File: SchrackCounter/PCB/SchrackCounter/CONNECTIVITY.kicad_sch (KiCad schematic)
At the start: 24 parts, among them J1 TYPE-C-31-M-12 (USB C CONN), U7 USBLC6-2SC6

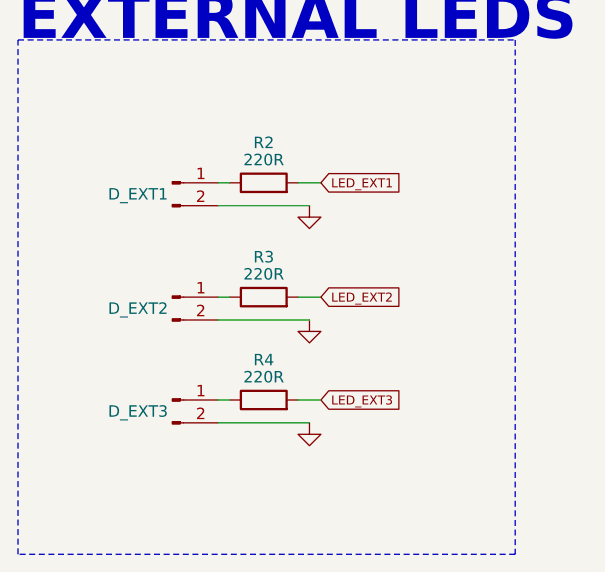
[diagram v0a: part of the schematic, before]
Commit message: SchrackMulticlock and Counter update
Schematic update for both
PCB update for Counter
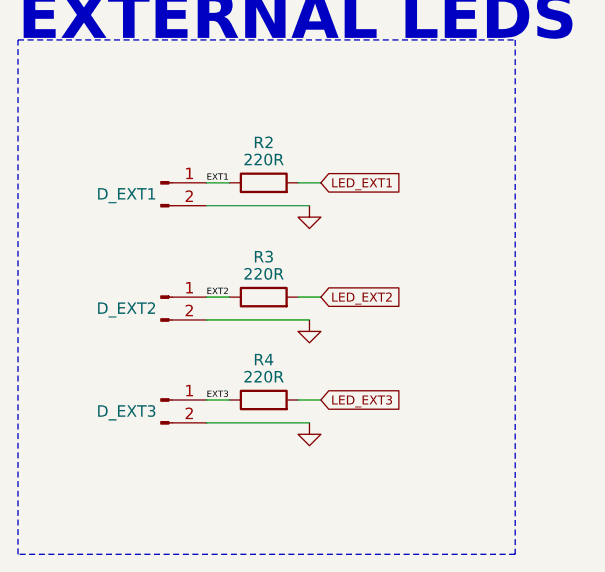
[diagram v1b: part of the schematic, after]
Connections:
- net EXT1: now reaches D_EXT1.1 (Pin_1), R2.1
- net EXT3: now reaches D_EXT3.1 (Pin_1), R4.1
- net EXT2: now reaches D_EXT2.1 (Pin_1), R3.1
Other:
- moved on the sheet: D_EXT1, D_EXT2, D_EXT3
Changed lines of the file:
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@@
 	(wire
 		(pts
-			(xy 78.74 142.24) (xy 77.47 142.24)
+			(xy 78.74 142.24) (xy 76.2 142.24)
 		)
 		(stroke
@@
 	(wire
 		(pts
-			(xy 78.74 118.11) (xy 77.47 118.11)
-		)
-		(stroke
-			(width 0)
-			(type default)
-		)
-	)
-	(wire
-		(pts
-			(xy 77.47 120.65) (xy 87.63 120.65)
+			(xy 76.2 120.65) (xy 87.63 120.65)
 		)
 		(stroke
@@
 	(wire
 		(pts
-			(xy 77.47 133.35) (xy 87.63 133.35)
+			(xy 76.2 133.35) (xy 87.63 133.35)
 		)
 		(stroke
@@
 	(wire
 		(pts
-			(xy 222.25 49.53) (xy 223.52 49.53)
+			(xy 76.2 118.11) (xy 78.74 118.11)
 		)
 		(stroke
@@
 	(wire
 		(pts
-			(xy 78.74 130.81) (xy 77.47 130.81)
+			(xy 222.25 49.53) (xy 223.52 49.53)
 		)
 		(stroke
@@
 	(wire
 		(pts
+			(xy 76.2 130.81) (xy 78.74 130.81)
+		)
+		(stroke
+			(width 0)
+			(type default)
+		)
+	)
+	(wire
+		(pts
 			(xy 223.52 137.16) (xy 223.52 147.32)
 		)
@@
 	(wire
 		(pts
-			(xy 77.47 144.78) (xy 87.63 144.78)
+			(xy 76.2 144.78) (xy 87.63 144.78)
 		)
 		(stroke
@@
 		)
 	)
+	(label "EXT2"
+		(at 76.2 130.81 0)
+		(fields_autoplaced yes)
+		(effects
+			(font
+				(size 0.7 0.7)
+			)
+			(justify left bottom)
+		)
+	)
+	(label "EXT3"
+		(at 76.2 142.24 0)
+		(fields_autoplaced yes)
+		(effects
+			(font
+				(size 0.7 0.7)
+			)
+			(justify left bottom)
+		)
+	)
+	(label "EXT1"
+		(at 76.2 118.11 0)
+		(fields_autoplaced yes)
+		(effects
+			(font
+				(size 0.7 0.7)
+			)
+			(justify left bottom)
+		)
+	)
 	(global_label "VBUS 5V"
 		(shape input)
@@
 	(symbol
 		(lib_id "Connector:Conn_01x02_Pin")
-		(at 72.39 118.11 0)
+		(at 71.12 118.11 0)
 		(unit 1)
 		(exclude_from_sim no)
@@
 		(dnp no)
 		(property "Reference" "D_EXT1"
-			(at 68.58 119.38 0)
+			(at 67.31 119.38 0)
 			(effects
 				(font
@@
 		)
 		(property "Value" "Conn_01x02_Pin"
-			(at 71.755 115.57 0)
+			(at 70.485 115.57 0)
 			(effects
 				(font
@@
 		)
 		(property "Footprint" "Connector_JST:JST_XH_B2B-XH-A_1x02_P2.50mm_Vertical"
-			(at 72.39 118.11 0)
+			(at 71.12 118.11 0)
 			(effects
 				(font
@@
 		)
 		(property "Datasheet" "~"
-			(at 72.39 118.11 0)
+			(at 71.12 118.11 0)
 			(effects
 				(font
@@
 		)
 		(property "Description" "Generic connector, single row, 01x02, script generated"
-			(at 72.39 118.11 0)
+			(at 71.12 118.11 0)
 			(effects
 				(font
@@
 	(symbol
 		(lib_id "Connector:Conn_01x02_Pin")
-		(at 72.39 142.24 0)
+		(at 71.12 142.24 0)
 		(unit 1)
 		(exclude_from_sim no)
@@
 		(dnp no)
 		(property "Reference" "D_EXT3"
-			(at 68.58 143.51 0)
+			(at 67.31 143.51 0)
 			(effects
 				(font
@@
 		)
 		(property "Value" "Conn_01x02_Pin"
-			(at 71.755 139.7 0)
+			(at 70.485 139.7 0)
 			(effects
 				(font
@@
 		)
 		(property "Footprint" "Connector_JST:JST_XH_B2B-XH-A_1x02_P2.50mm_Vertical"
-			(at 72.39 142.24 0)
+			(at 71.12 142.24 0)
 			(effects
 				(font
@@
 		)
 		(property "Datasheet" "~"
-			(at 72.39 142.24 0)
+			(at 71.12 142.24 0)
 			(effects
 				(font
@@
 		)
 		(property "Description" "Generic connector, single row, 01x02, script generated"
-			(at 72.39 142.24 0)
+			(at 71.12 142.24 0)
 			(effects
 				(font
@@
 	(symbol
 		(lib_id "Connector:Conn_01x02_Pin")
-		(at 72.39 130.81 0)
+		(at 71.12 130.81 0)
 		(unit 1)
 		(exclude_from_sim no)
@@
 		(dnp no)
 		(property "Reference" "D_EXT2"
-			(at 68.58 132.08 0)
+			(at 67.31 132.08 0)
 			(effects
 				(font
@@
 		)
 		(property "Value" "Conn_01x02_Pin"
-			(at 71.755 128.27 0)
+			(at 70.485 128.27 0)
 			(effects
 				(font
@@
 		)
 		(property "Footprint" "Connector_JST:JST_XH_B2B-XH-A_1x02_P2.50mm_Vertical"
-			(at 72.39 130.81 0)
+			(at 71.12 130.81 0)
 			(effects
 				(font
@@
 		)
 		(property "Datasheet" "~"
-			(at 72.39 130.81 0)
+			(at 71.12 130.81 0)
 			(effects
 				(font
@@
 		)
 		(property "Description" "Generic connector, single row, 01x02, script generated"
-			(at 72.39 130.81 0)
+			(at 71.12 130.81 0)
 			(effects
 				(font

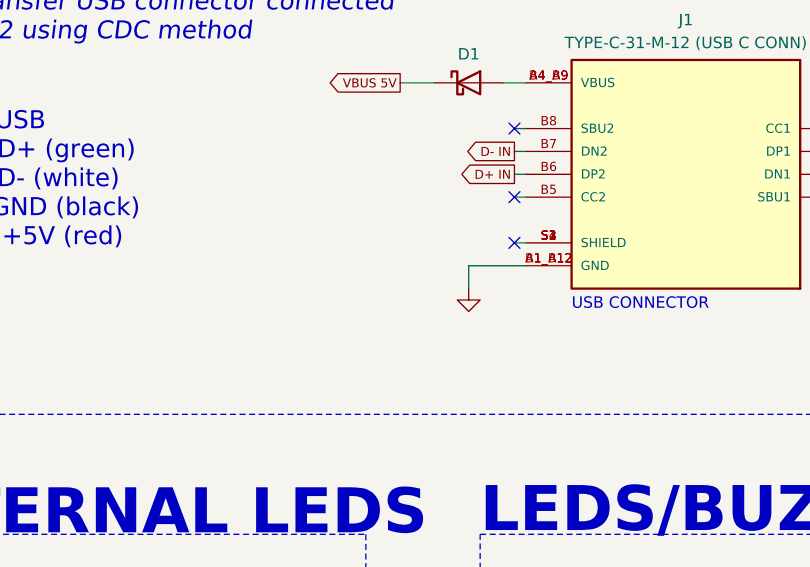
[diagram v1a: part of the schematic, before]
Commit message: Schrackcounter Prototype update
Schematic + PCB update, final version
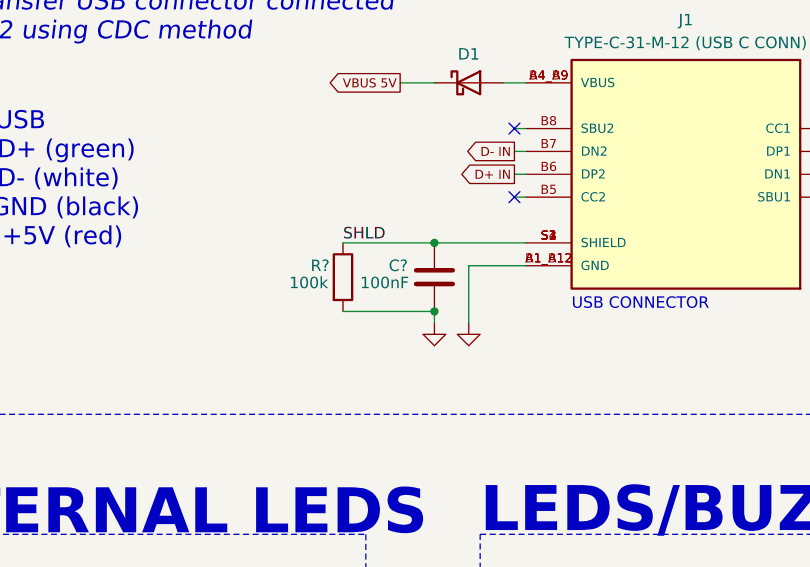
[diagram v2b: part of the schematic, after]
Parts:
- added C?: 100nF, Capacitor_SMD:C_0805_2012Metric_Pad1.18x1.45mm_HandSolder, symbol Device:C
- added R?: 100k, Resistor_SMD:R_0805_2012Metric_Pad1.20x1.40mm_HandSolder, symbol Device:R
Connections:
- net GND: now also C?.1, R?.2
- net SHLD: now reaches J1.S1 (SHIELD), J1.S2 (SHIELD), J1.S3 (SHIELD), J1.S4 (SHIELD)
- net SHLD: now also C?.2, R?.1
- no-connect marks 5 -> 4

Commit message: SchrackMulticlock update
Schematic and PCB update
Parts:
- gave numbers to parts that had none: 2
- renumbered C9 to C10, R9 to R10, R10 to R11, R11 to R12, R5 to R6, R6 to R7, R7 to R8, R8 to R9

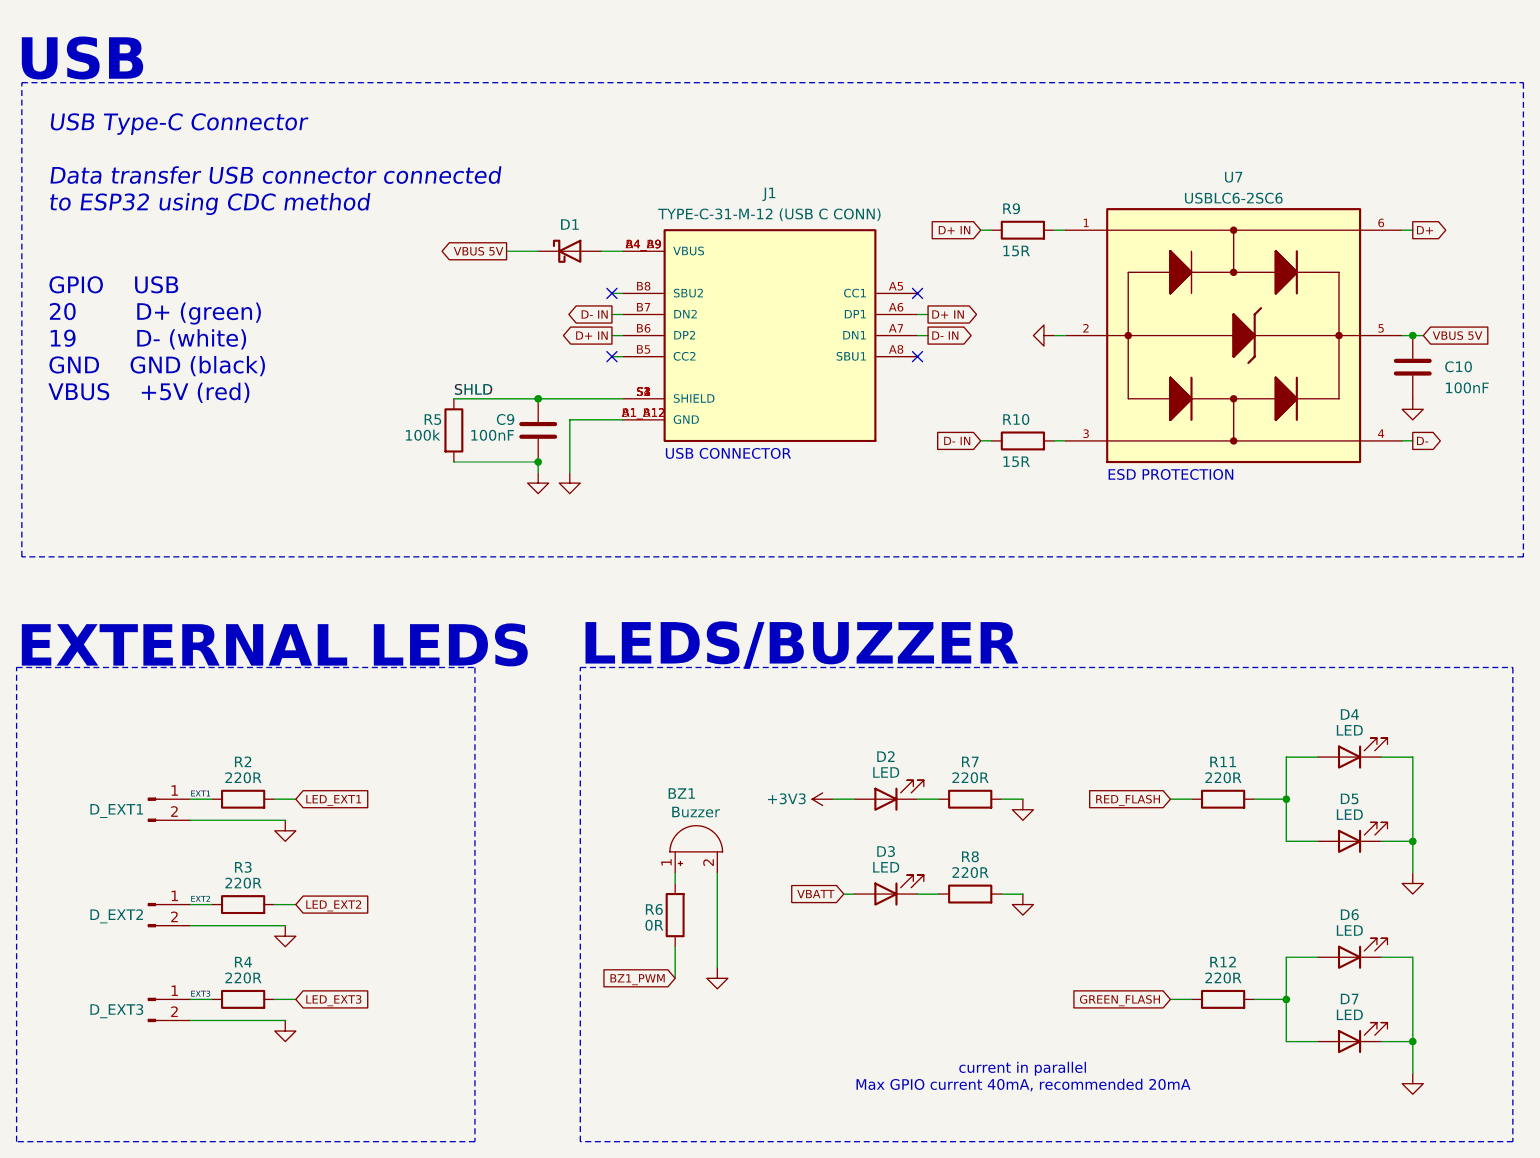
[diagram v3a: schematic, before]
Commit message: SchrackCounter update - FIX
USB footprint standoff fix
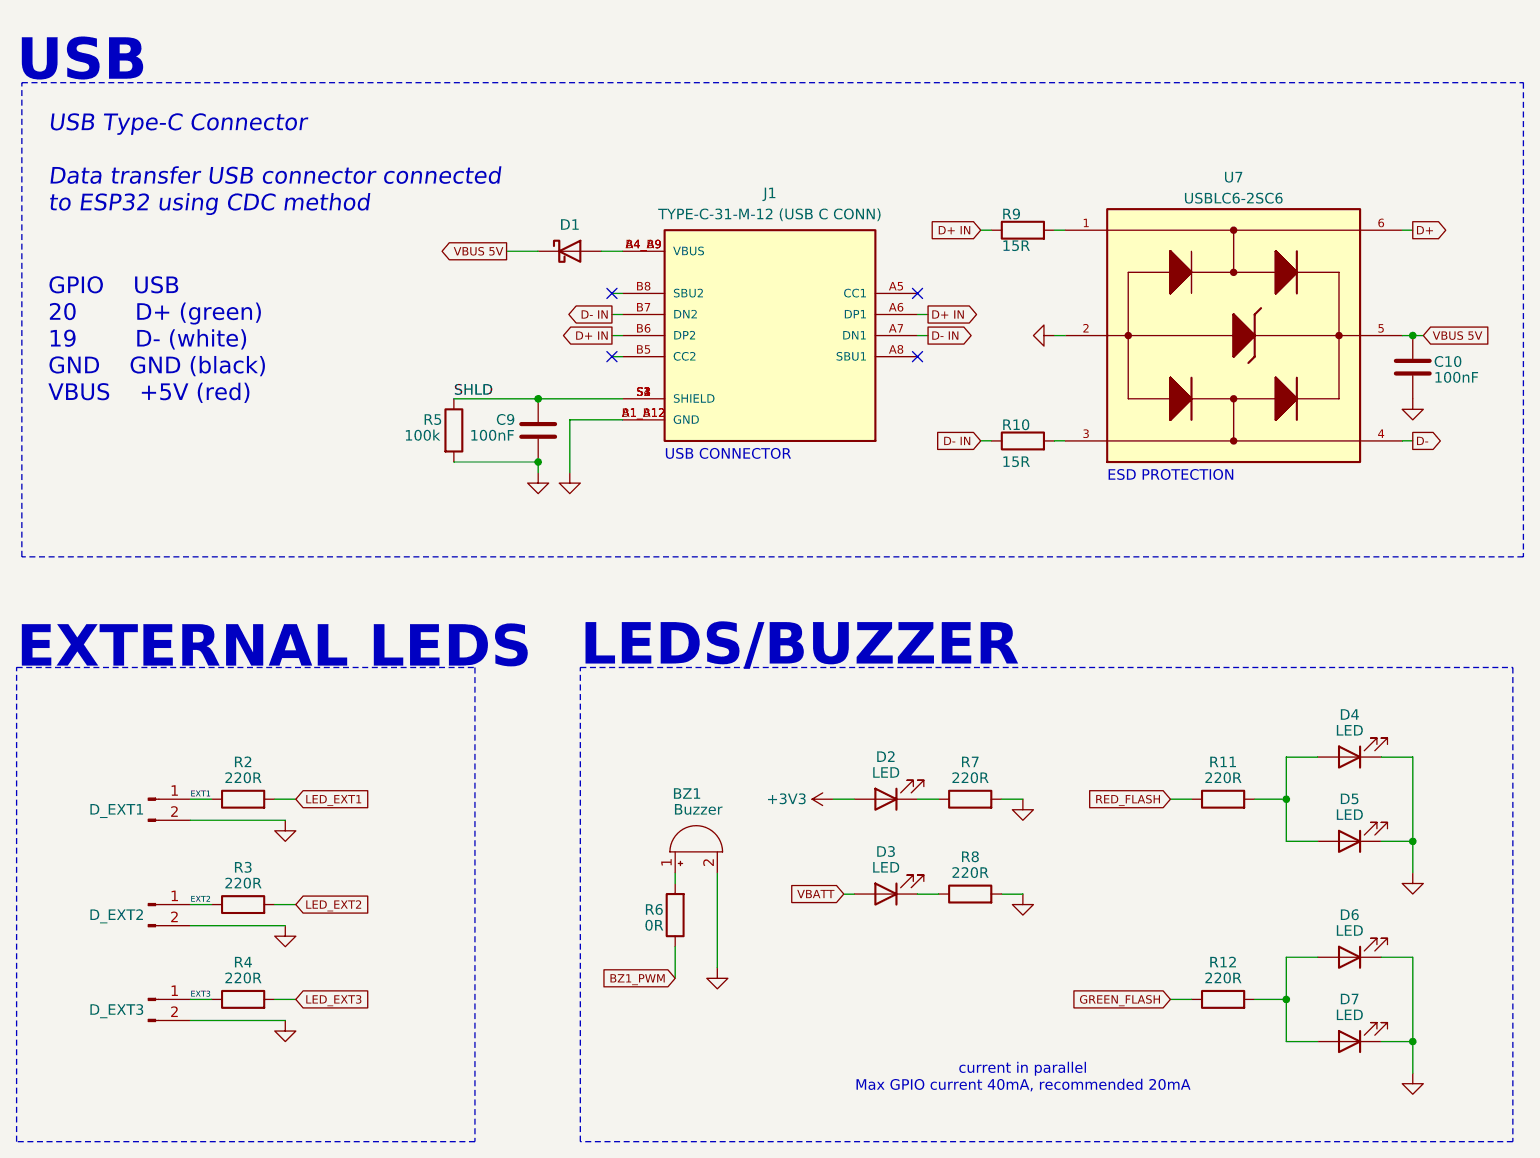
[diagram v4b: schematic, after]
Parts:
- J1: footprint sumec_brd:USB_Type_C -> sumec_brd:HRO_TYPE-C-31-M-12
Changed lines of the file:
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@@
 		(dnp no)
 		(property "Reference" "BZ1"
-			(at 137.16 117.475 90)
+			(at 137.795 117.475 90)
 			(effects
 				(font
@@
 		)
 		(property "Value" "Buzzer"
-			(at 140.0175 119.6976 90)
+			(at 140.335 119.38 90)
 			(effects
 				(font
@@
 		(dnp no)
 		(property "Reference" "R10"
-			(at 173.99 72.39 90)
+			(at 173.99 73.025 90)
 			(effects
 				(font
@@
 			)
 		)
-		(property "Footprint" "sumec_brd:USB_Type_C"
+		(property "Footprint" "sumec_brd:HRO_TYPE-C-31-M-12"
 			(at 146.05 62.23 0)
 			(effects
@@
 		(dnp no)
 		(property "Reference" "R9"
-			(at 173.99 46.99 90)
+			(at 173.99 47.625 90)
 			(effects
 				(font
@@
 		)
 		(property "Value" "15R"
-			(at 173.99 52.07 90)
+			(at 173.99 51.435 90)
 			(effects
 				(font
@@
 		(dnp no)
 		(property "Reference" "C10"
-			(at 227.33 66.04 0)
+			(at 226.06 65.405 0)
 			(effects
 				(font
@@
 		)
 		(property "Value" "100nF"
-			(at 227.33 68.58 0)
-			(effects
-				(font
+			(at 226.06 67.31 0)
+			(effects
+				(font

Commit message: SchrackMulticlock and Counter pcb updates
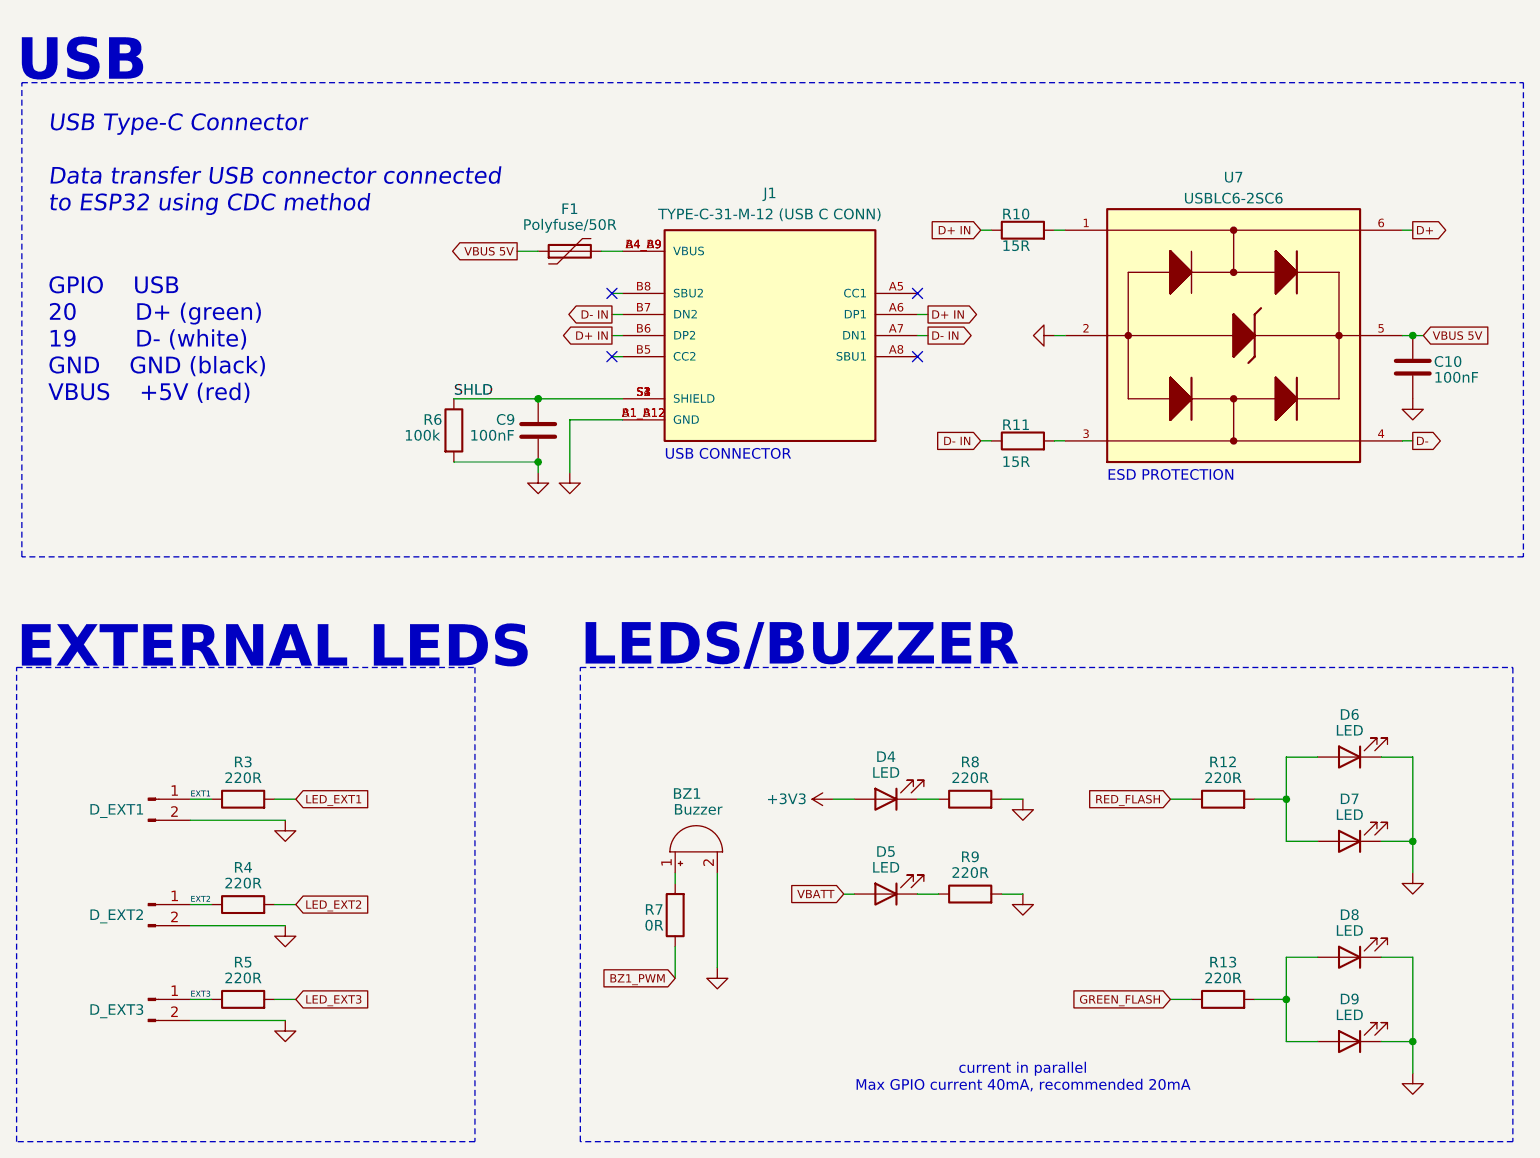
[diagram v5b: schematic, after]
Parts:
- removed D1: D_Schottky, Diode_SMD:D_1206_3216Metric_Pad1.42x1.75mm_HandSolder, symbol Device:D_Schottky
- added F1: Polyfuse/50R, Fuse:Fuse_0805_2012Metric, symbol Device:Polyfuse
- renumbered D2 to D4, D3 to D5, D4 to D6, D5 to D7, D6 to D8, D7 to D9, R9 to R10, R10 to R11, R11 to R12, R12 to R13, R2 to R3, R3 to R4, R4 to R5, R5 to R6, R6 to R7, R7 to R8, R8 to R9
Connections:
- net VBUS 5V: now also F1.1
- net at J1.A4_B9 (VBUS), J1.B4_A9 (VBUS): now also F1.2
